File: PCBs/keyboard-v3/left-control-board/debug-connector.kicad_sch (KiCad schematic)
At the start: 1 part, among them J501 Conn_02x08_Odd_Even

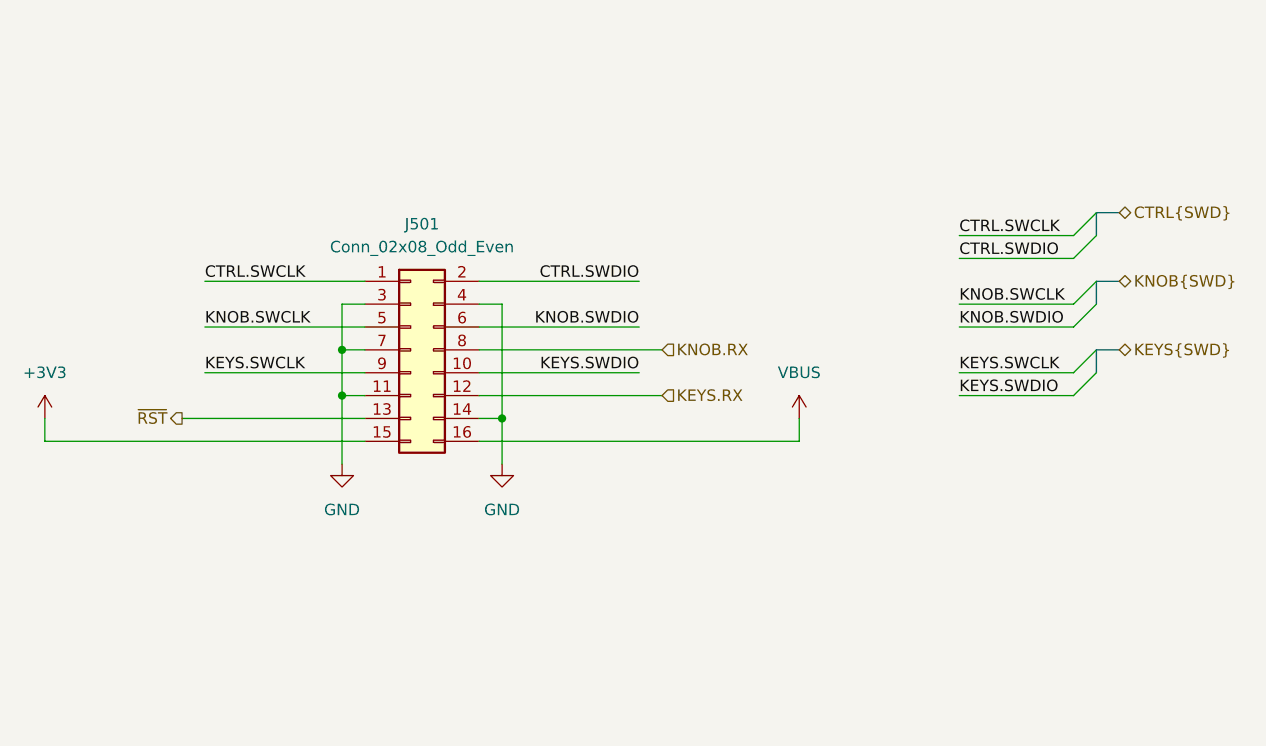
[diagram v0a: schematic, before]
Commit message: Added debug-breakout board, progress on right side schematics & layout
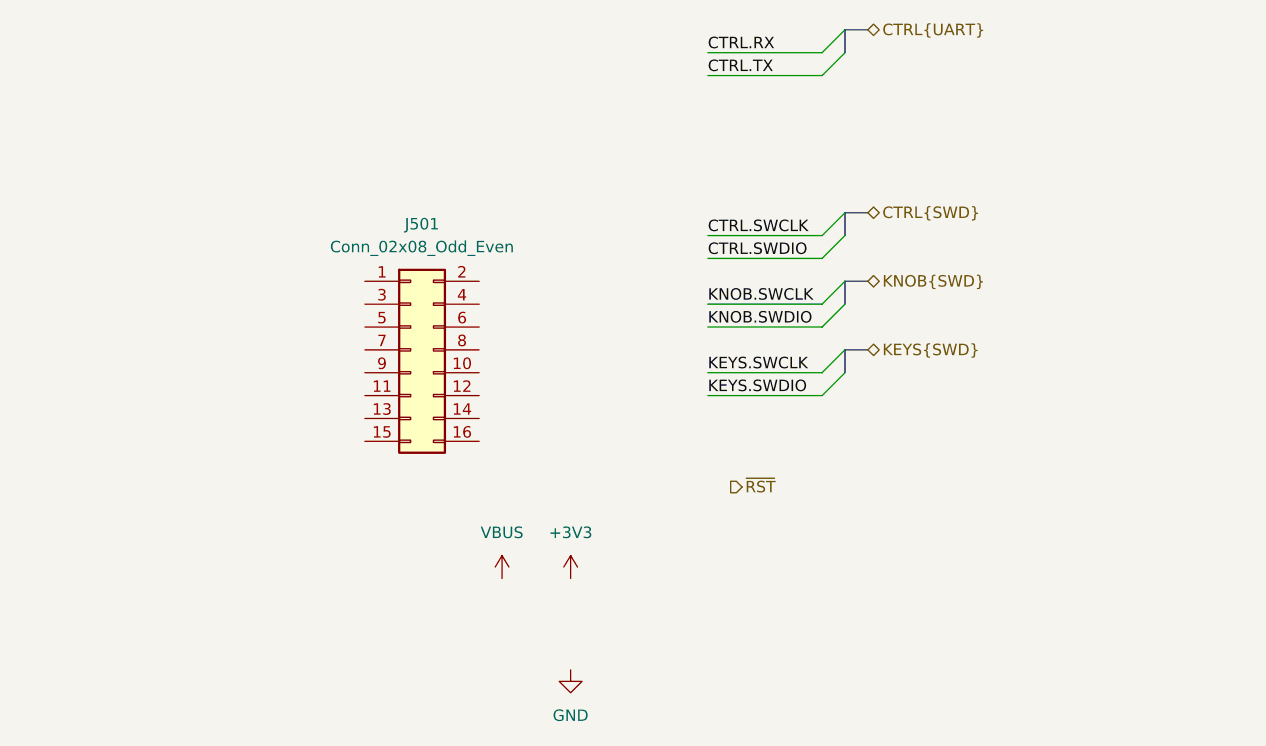
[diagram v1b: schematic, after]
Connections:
- net +3V3: no longer J501.15 (Pin_15)
- net CTRL.SWCLK: no longer J501.1 (Pin_1)
- net CTRL.SWDIO: no longer J501.2 (Pin_2)
- net GND: no longer J501.11 (Pin_11), J501.14 (Pin_14), J501.3 (Pin_3), J501.4 (Pin_4), J501.7 (Pin_7)
- net KEYS.SWCLK: no longer J501.9 (Pin_9)
- net KEYS.SWDIO: no longer J501.10 (Pin_10)
- net KNOB.SWCLK: no longer J501.5 (Pin_5)
- net KNOB.SWDIO: no longer J501.6 (Pin_6)
- net VBUS: no longer J501.16 (Pin_16)
- net ~{RST}: no longer J501.13 (Pin_13)
- net KEYS.RX: no longer names the net of J501.12 (Pin_12)
- net KNOB.RX: no longer names the net of J501.8 (Pin_8)

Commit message: Left knob board done
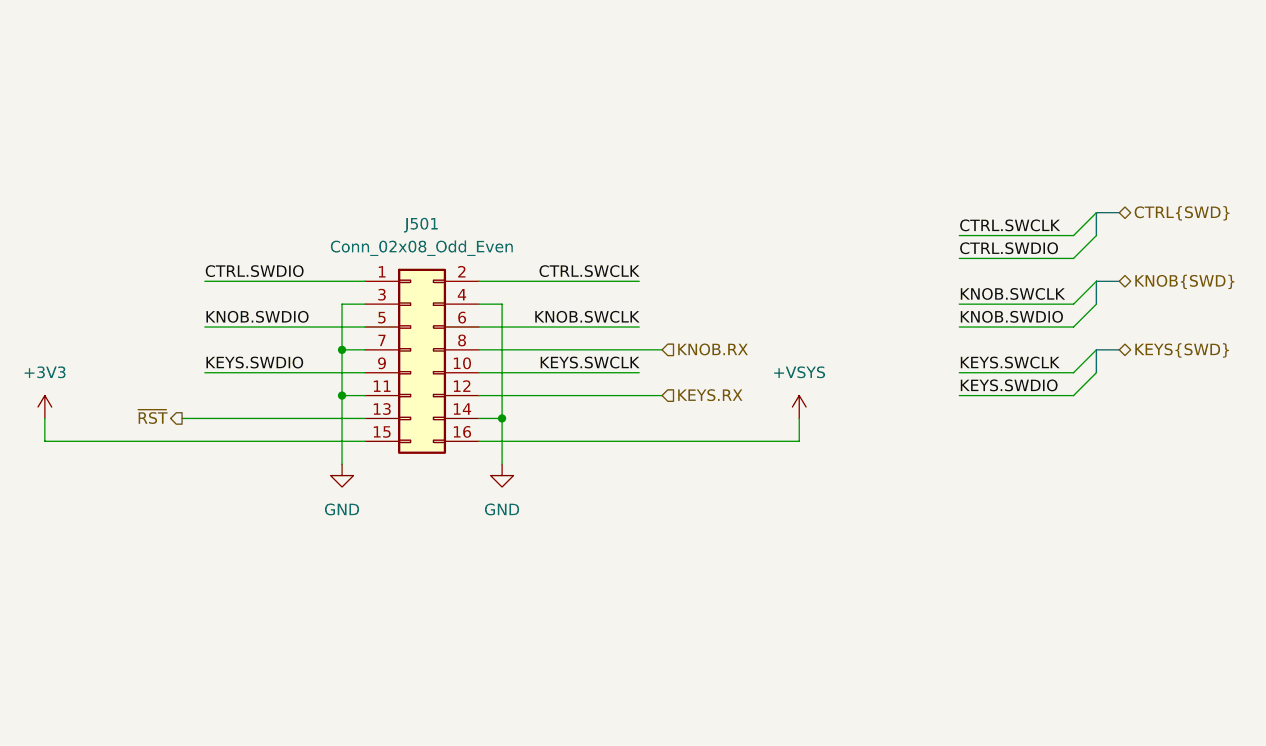
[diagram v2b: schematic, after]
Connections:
- net +3V3: now also J501.15 (Pin_15)
- net CTRL.SWCLK: now also J501.2 (Pin_2)
- net CTRL.SWDIO: now also J501.1 (Pin_1)
- net GND: now also J501.11 (Pin_11), J501.14 (Pin_14), J501.3 (Pin_3), J501.4 (Pin_4), J501.7 (Pin_7)
- net KEYS.SWCLK: now also J501.10 (Pin_10)
- net KEYS.SWDIO: now also J501.9 (Pin_9)
- net KNOB.SWCLK: now also J501.6 (Pin_6)
- net KNOB.SWDIO: now also J501.5 (Pin_5)
- net ~{RST}: now also J501.13 (Pin_13)
- net KEYS.RX: now reaches J501.12 (Pin_12)
- net +VSYS: now reaches J501.16 (Pin_16)
- net KNOB.RX: now reaches J501.8 (Pin_8)
